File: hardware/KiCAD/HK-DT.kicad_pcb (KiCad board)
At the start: 2 copper layers, 58 x 38 mm, 32 parts, among them J1 USB_B_Micro, Q1 Q_0001, SW1 SW_0003, U1 BME280, U2 CH340G, U3 ESP-12E, U5 TLV61225, U6 U_0037, U7 U_0049

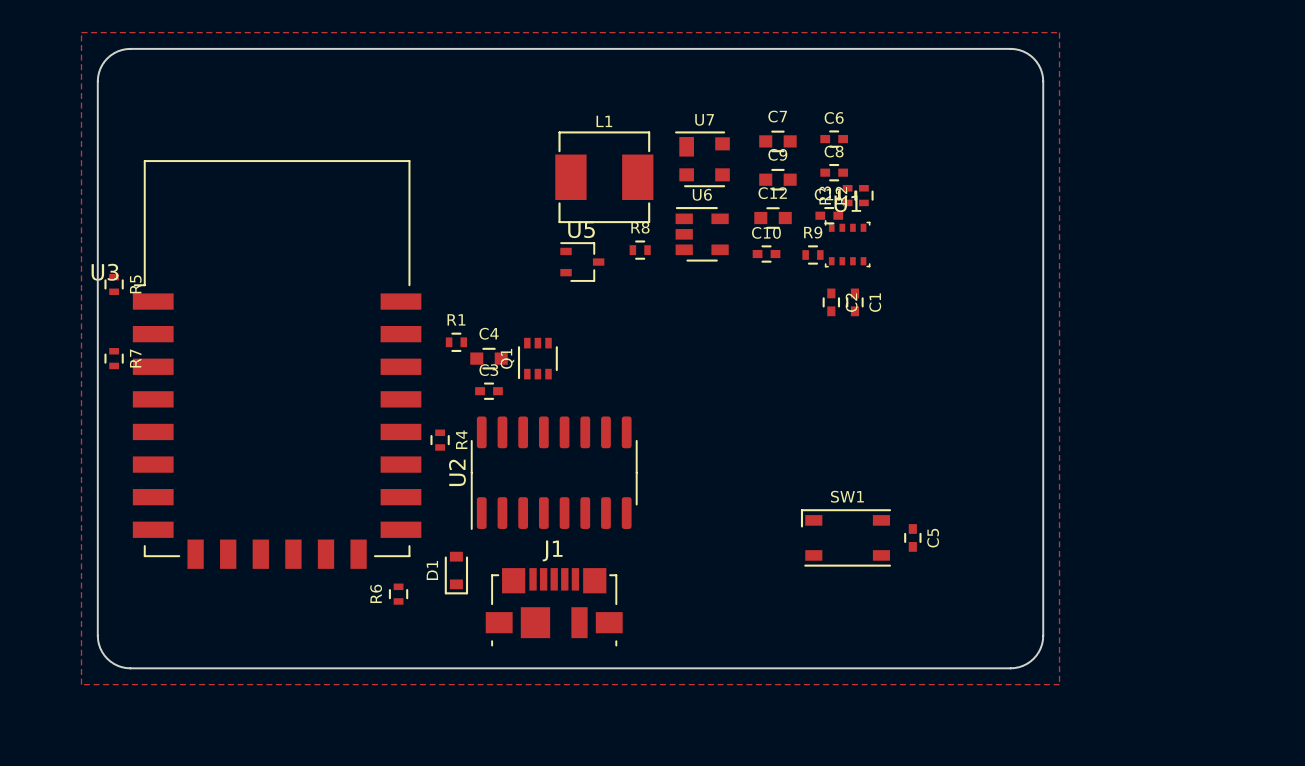
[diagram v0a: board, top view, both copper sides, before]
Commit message: cleaning schematic / Routing started (Power line mostly done), need to change USB footprint & make 3D Model / Footprint of OLED
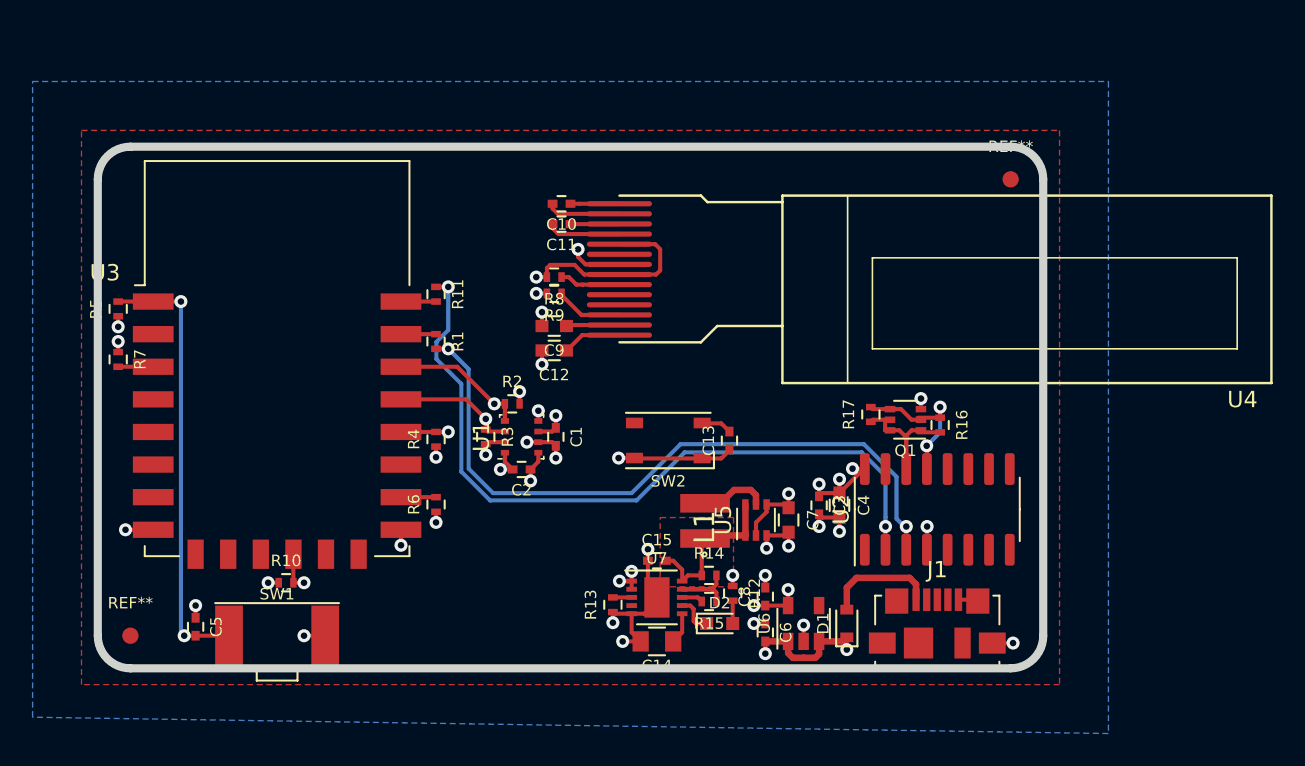
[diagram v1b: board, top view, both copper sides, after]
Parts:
- added C13: C_0002, DVB_Capacitors_Ceramic:C_0402, F.Cu at (86.8, 127.0)
- added C14: C_0060, DVB_Capacitors_Ceramic:C_0805, F.Cu at (82.3, 139.4)
- added C15: C_0044, DVB_Capacitors_Ceramic:C_0402, F.Cu at (82.3, 134.4)
- added D2: D_0001, DVB_LED:LED_0603-red, F.Cu at (86.1, 138.2)
- added R10: 10k, DVB_Resistors:R_0402, F.Cu at (59.5, 135.8)
- added R11: 470, DVB_Resistors:R_0402, F.Cu at (68.8, 118.0)
- added R12: R_0005, DVB_Resistors:R_0402, F.Cu at (87.0, 136.4)
- added R13: R_0140, DVB_Resistors:R_0402, F.Cu at (79.6, 137.1)
- added R14: 324k, DVB_Resistors:R_0402, F.Cu at (85.5, 135.3)
- added R15: 178k, DVB_Resistors:R_0402, F.Cu at (85.5, 136.9)
- added R16: 10k, DVB_Resistors:R_0402, F.Cu at (99.7, 126.1)
- added R17: 10k, DVB_Resistors:R_0402, F.Cu at (95.4, 125.4)
- added REF**: CircleWhite1mm, DVB_Fiducials:REF_1mm, F.Cu at (104.0, 111.0)
- added REF**: CircleWhite1mm, DVB_Fiducials:REF_1mm, F.Cu at (50.0, 139.0)
- added SW2: SW_0003, DVB_Buttons:PTS810, F.Cu at (83.0, 127.0)
- added U4: SSD1306, HK-DT:ssd1306, F.Cu at (120.0, 123.5)
- L1: footprint DVB_Inductors:L_2020-Vishay -> HK-DT:LPS3015
- SW1: value SW_0003 -> SW_0002; footprint DVB_Buttons:PTS810 -> DVB_Buttons:KSS221G
- U5: footprint Package_TO_SOT_SMD:SOT-323_SC-70 -> Package_TO_SOT_SMD:SOT-363_SC-70-6
- U7: value U_0049 -> U_0104; footprint DVB_SOT:SOT_143 -> DVB_DFN:DFN_10-1EP_3x3mm_P0.5mm
- moved C5 44.3 mm to (54.0, 138.4)
- moved SW1 35.5 mm to (59.0, 139.0)
- moved C6 30.6 mm to (89.0, 138.8), turned to 270 degrees
- moved U7 27.0 mm to (82.3, 136.7)
- moved R3 26.7 mm to (71.8, 126.8), turned to 270 degrees
- moved C8 26.3 mm to (89.0, 136.6), turned to 90 degrees
- moved R2 25.1 mm to (73.4, 124.8), turned to 0 degrees
- moved U6 24.7 mm to (91.3, 138.2), turned to 90 degrees
- moved D1 24.2 mm to (94.0, 138.2)
- moved U2 23.6 mm to (99.5, 131.2)
- moved J1 23.5 mm to (99.5, 138.2)
- moved C4 23.3 mm to (93.5, 131.0), turned to 270 degrees
- moved C7 23.2 mm to (90.4, 131.9), turned to 270 degrees
- moved U1 23.2 mm to (74.0, 126.8), turned to 90 degrees
- moved Q1 22.9 mm to (97.5, 125.8), turned to 180 degrees
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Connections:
- C10 pad 1: (no net) -> Net-(C10-Pad1)
- C10 pad 2: (no net) -> Net-(C10-Pad2)
- C11 pad 1: (no net) -> Net-(C11-Pad1)
- C11 pad 2: (no net) -> Net-(C11-Pad2)
- C12 pad 1: (no net) -> Net-(C12-Pad1)
- C9 pad 1: (no net) -> Net-(C9-Pad1)
- L1 pad 1: (no net) -> +BATT
- L1 pad 2: (no net) -> Net-(L1-Pad2)
- R4 pad 1: /GPIO0 -> +3V3
- R4 pad 2: +3V3 -> /GPIO0
- R6 pad 1: (no net) -> GND
- R6 pad 2: GND -> Net-(R6-Pad2)
- R8 pad 1: (no net) -> Net-(R8-Pad1)
- R9 pad 1: (no net) -> Net-(R9-Pad1)
- SW1 pad 1: GND -> /RST
- U2 pad 2: /Tx -> Net-(R11-Pad1)
- U3 pad 12: (no net) -> /BP
- U3 pad 16: (no net) -> Net-(R6-Pad2)
- U3 pad 19: (no net) -> /SDA
- U3 pad 20: (no net) -> /SCL
- U5 pad 1: (no net) -> +BATT
- U5 pad 2: (no net) -> +3V3
- U5 pad 3: (no net) -> GND
- U7 pad 1: GND -> +5V
- U7 pad 2: /SCL -> +5V
- U7 pad 3: /SDA -> Net-(R13-Pad2)
- U7 pad 4: +3V3 -> (no net)
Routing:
- net Net-(R11-Pad1): track 0.00 -> 46.1 mm, vias 0 -> 2
- net Net-(R1-Pad2): track 0.00 -> 42.4 mm, vias 0 -> 2
- net GND: track 0.00 -> 39.7 mm, vias 0 -> 23
- net +3V3: track 0.00 -> 38.1 mm, vias 0 -> 17
- net /RST: track 0.00 -> 27.2 mm, vias 0 -> 2
- net +5V: track 0.00 -> 10.8 mm, vias 0 -> 5
- net +BATT: track 0.00 -> 10.1 mm
- net /~DTR: track 0.00 -> 9.82 mm, vias 0 -> 2
- net /~RST: track 0.00 -> 9.71 mm
- net /BP: track 0.00 -> 9.22 mm, vias 0 -> 2
- net /SCL: track 0.00 -> 8.43 mm, vias 0 -> 1
- net /SDA: track 0.00 -> 7.57 mm, vias 0 -> 1
- net Net-(D1-Pad2): track 0.00 -> 6.95 mm
- net Net-(R14-Pad2): track 0.00 -> 5.51 mm
- net Net-(C10-Pad2): track 0.00 -> 4.53 mm
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- added copper zone on VCC, net +3V3
- added copper zone on VCC, net +5V
- added copper zone on F.Cu, net +BATT
- added copper zone on B.Cu, net GND
- added copper zone on GND, net GND
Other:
- board size 58 x 38 mm -> 58 x 32 mm
- copper layers 2 -> 4
- board text added: "CoBox v1.0.0"
- board text added: "RST"
- board text removed: "HomeKit CoBox v1.0.0"

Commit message: Change footprint USB - Fix OLED Display Footprint
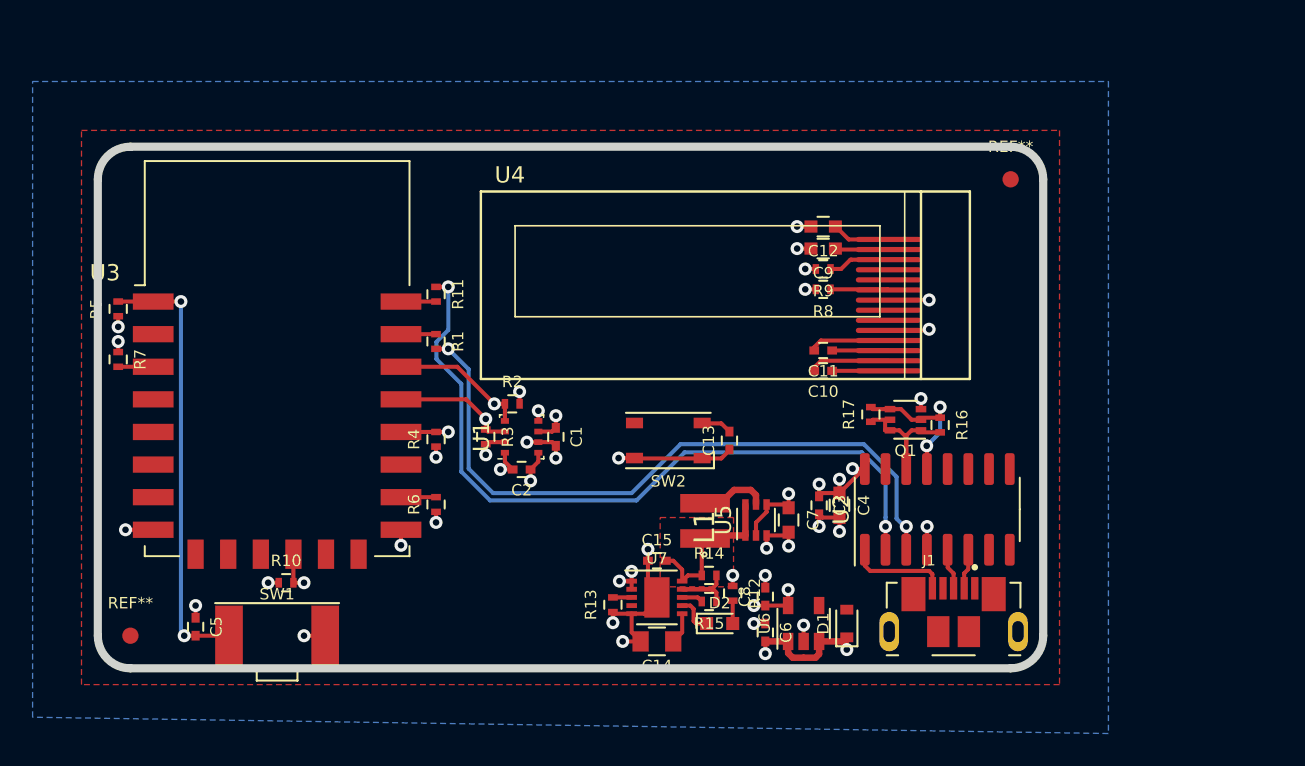
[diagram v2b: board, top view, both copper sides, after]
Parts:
- J1: footprint Connector_USB:USB_Micro-B_Molex_47346-0001 -> HK-DT:MOLEX_105164-0001
- moved U4 49.9 mm to (71.5, 111.8), turned to 0 degrees
- moved C10 19.0 mm to (92.5, 122.8)
- moved C12 18.2 mm to (92.5, 113.9)
- moved C11 17.8 mm to (92.5, 121.5)
- moved C9 17.2 mm to (92.5, 115.2)
- moved R9 16.6 mm to (92.5, 116.5)
- moved R8 16.5 mm to (92.5, 117.8)
- moved J1 2.19 mm to (100.5, 140.2)
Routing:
- net Net-(D1-Pad2): track 6.95 -> 0.00 mm
- net +3V3: track 38.1 -> 31.3 mm, vias 17 -> 19
- net /D+: track 0.00 -> 2.52 mm
- net /D-: track 0.00 -> 2.47 mm
- net GND: track 39.7 -> 40.2 mm, vias 23 -> 21

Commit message: Add BatteryHolder Footprint & 3D, routing done, need to move power section to left
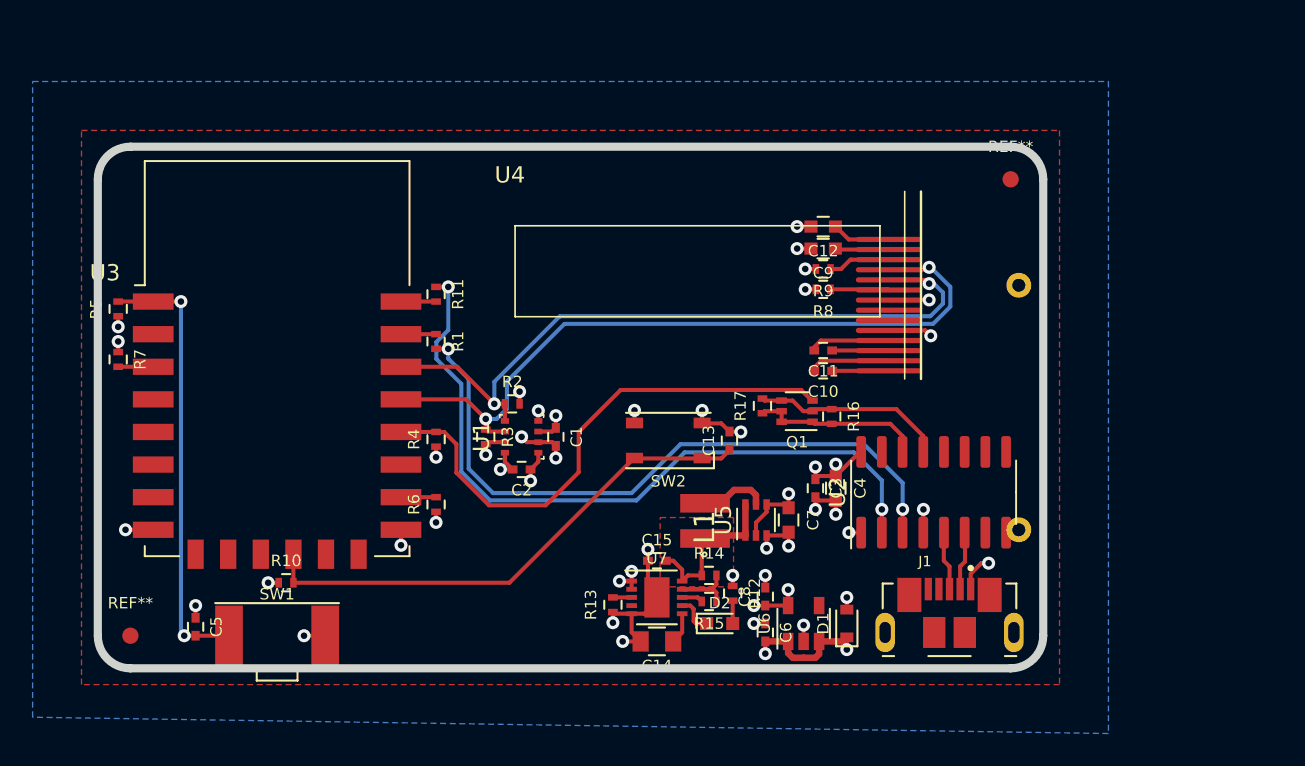
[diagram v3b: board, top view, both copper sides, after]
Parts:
- added BT1: Battery, HK-DT:2462, B.Cu at (76.2, 125.0)
- added G***: LOGO, HK-DT:cow, F.Cu at (75.8, 138.0)
- moved Q1 6.67 mm to (90.9, 125.2)
- moved R17 6.67 mm to (88.8, 124.9)
- moved R16 6.67 mm to (93.0, 125.5)
- moved C3 1.07 mm to (92.0, 129.9)
- moved C4 1.07 mm to (93.3, 129.9)
- moved U2 1.07 mm to (99.3, 130.2)
- moved J1 0.25 mm to (100.2, 140.2)
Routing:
- net /SDA: track 7.57 -> 45.5 mm, vias 1 -> 2
- net /SCL: track 8.43 -> 43.6 mm, vias 1 -> 2
- net /GPIO0: track 3.55 -> 32.8 mm, vias 2 -> 0
- net /BP: track 9.22 -> 31.7 mm, vias 2 -> 0
- net Net-(D1-Pad2): track 0.00 -> 3.06 mm, vias 0 -> 2
- net GND: track 40.2 -> 37.4 mm, vias 21 -> 25
- net /~DTR: track 9.82 -> 12.3 mm, vias 2 -> 0
- net Net-(R11-Pad1): track 46.1 -> 44.7 mm
- net Net-(R1-Pad2): track 42.4 -> 41.1 mm
- net /D-: track 2.47 -> 3.60 mm
- net /D+: track 2.52 -> 3.61 mm
- net /~RST: track 9.71 -> 10.6 mm
- net +3V3: track 31.3 -> 30.6 mm, vias 19 -> 18
- added copper zone on VCC, net Net-(D1-Pad2)
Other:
- board text added: "v1.0.0"
- board text removed: "CoBox v1.0.0"
- board text removed: "UART CHRG"

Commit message: Power placement is ok, need to change pinout battery holder
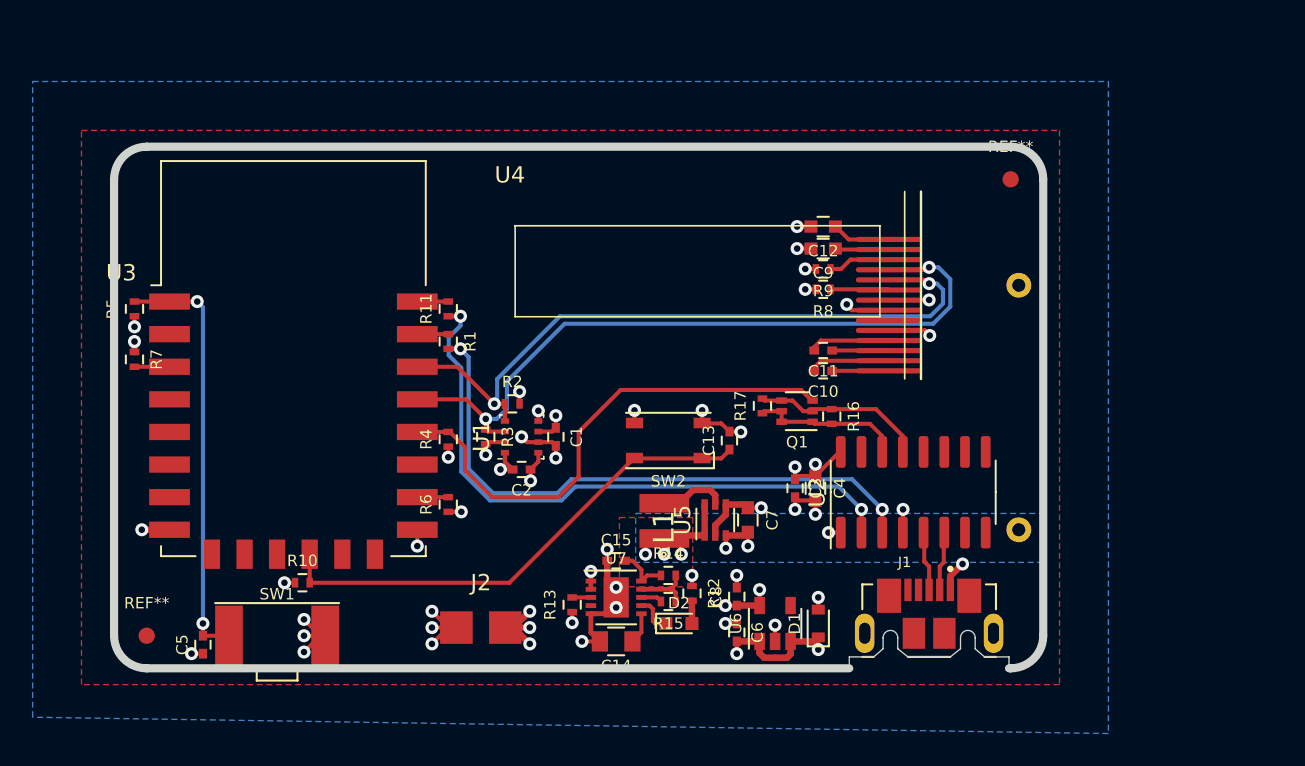
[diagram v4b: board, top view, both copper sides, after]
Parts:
- removed G***: LOGO, HK-DT:cow
- added J2: Pad_1x2, HK-DT:DualPad, F.Cu at (71.5, 138.5)
- moved C14 2.50 mm to (79.8, 139.4)
- moved C15 2.50 mm to (79.8, 134.4)
- moved C7 2.50 mm to (87.9, 131.9)
- moved D2 2.50 mm to (83.6, 138.2)
- moved L1 2.50 mm to (82.8, 132.0)
- moved R12 2.50 mm to (84.5, 136.4)
- moved R13 2.50 mm to (77.1, 137.1)
- moved R14 2.50 mm to (83.0, 135.3)
- moved R15 2.50 mm to (83.0, 136.9)
- moved U5 2.50 mm to (85.9, 131.9)
- moved U7 2.50 mm to (79.8, 136.7)
- moved C6 1.75 mm to (87.2, 138.8)
- moved C8 1.75 mm to (87.2, 136.6)
- moved D1 1.75 mm to (92.2, 138.2)
- moved U6 1.75 mm to (89.5, 138.2)
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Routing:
- net GND: track 37.4 -> 48.0 mm, vias 25 -> 33
- net Net-(R11-Pad1): track 44.7 -> 38.5 mm
- net Net-(R1-Pad2): track 41.1 -> 36.8 mm
- net +5V: track 10.8 -> 14.9 mm, vias 5 -> 7
- net Net-(R6-Pad2): track 2.15 -> 4.05 mm
- net /Tx: track 2.15 -> 4.05 mm
- net /Rx: track 2.15 -> 4.05 mm
- net /~DTR: track 12.3 -> 11.0 mm
- net /~RST: track 10.6 -> 9.38 mm
- net +BATT: track 10.1 -> 8.98 mm, vias 0 -> 3
- net /BP: track 31.7 -> 30.7 mm
- net /GPIO0: track 32.8 -> 32.1 mm
- net /RST: track 27.2 -> 27.8 mm
- added copper zone on B.Cu, net +BATT
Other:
- board size 58 x 32 mm -> 57 x 32 mm
- board text added: "+"
- board text added: "-"
- board text removed: "v1.0.0"

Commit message: Change Pads Battery holder, Add decoupling capacitor
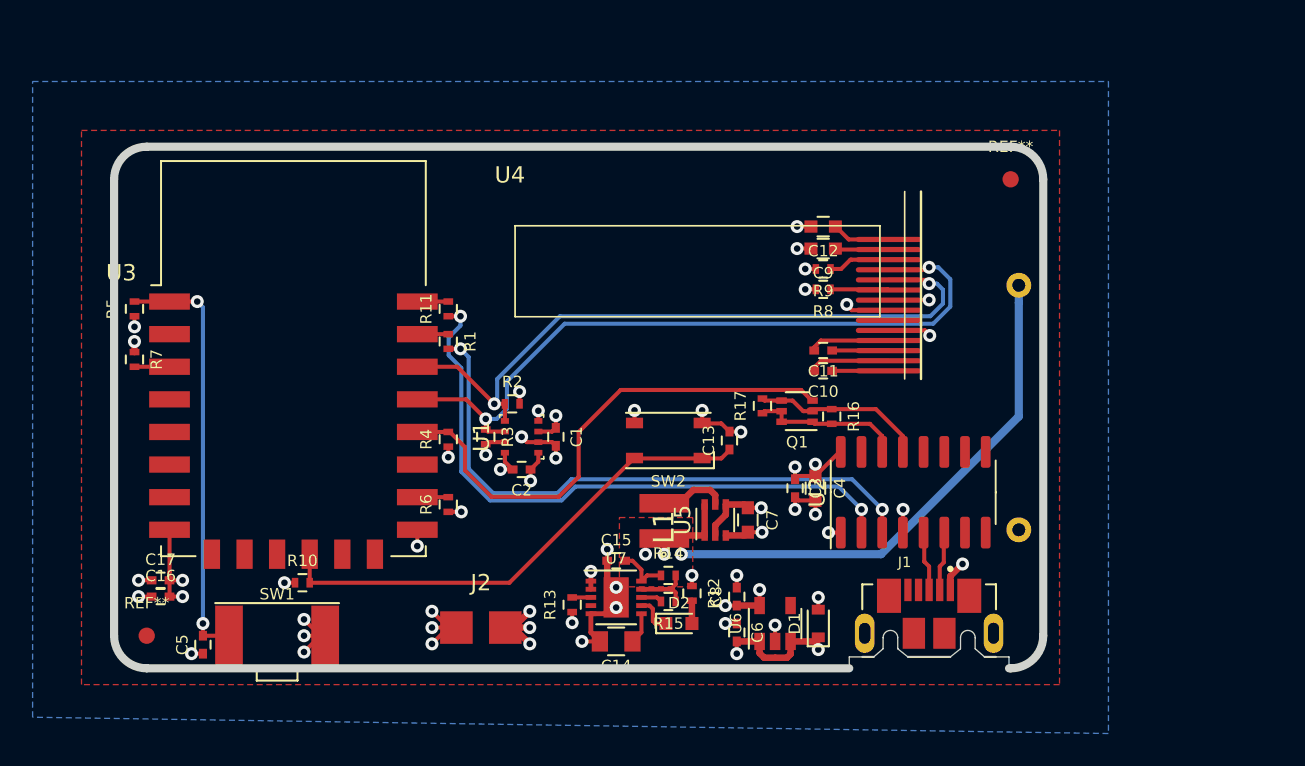
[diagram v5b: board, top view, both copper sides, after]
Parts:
- added C16: C_0002, DVB_Capacitors_Ceramic:C_0402, F.Cu at (51.9, 136.6)
- added C17: C_0002, DVB_Capacitors_Ceramic:C_0402, F.Cu at (51.9, 135.6)
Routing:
- net +BATT: track 8.98 -> 41.2 mm
- net +3V3: track 30.5 -> 34.5 mm, vias 18 -> 19
- net GND: track 48.0 -> 48.8 mm, vias 33 -> 34
- removed copper zone on B.Cu, net +BATT
